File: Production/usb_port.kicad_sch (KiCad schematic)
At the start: 96 parts, among them J401 TYPE-C 16PCB1.6 IP68, Q401 SiZ240DT, Q402 SiZ240DT, U401 TPS25751DREFR, U402 M24512-DFMC6TG, U403 BQ25756RRVR, U404 TPS62933DRLR, U405 TPD6S300RUKR

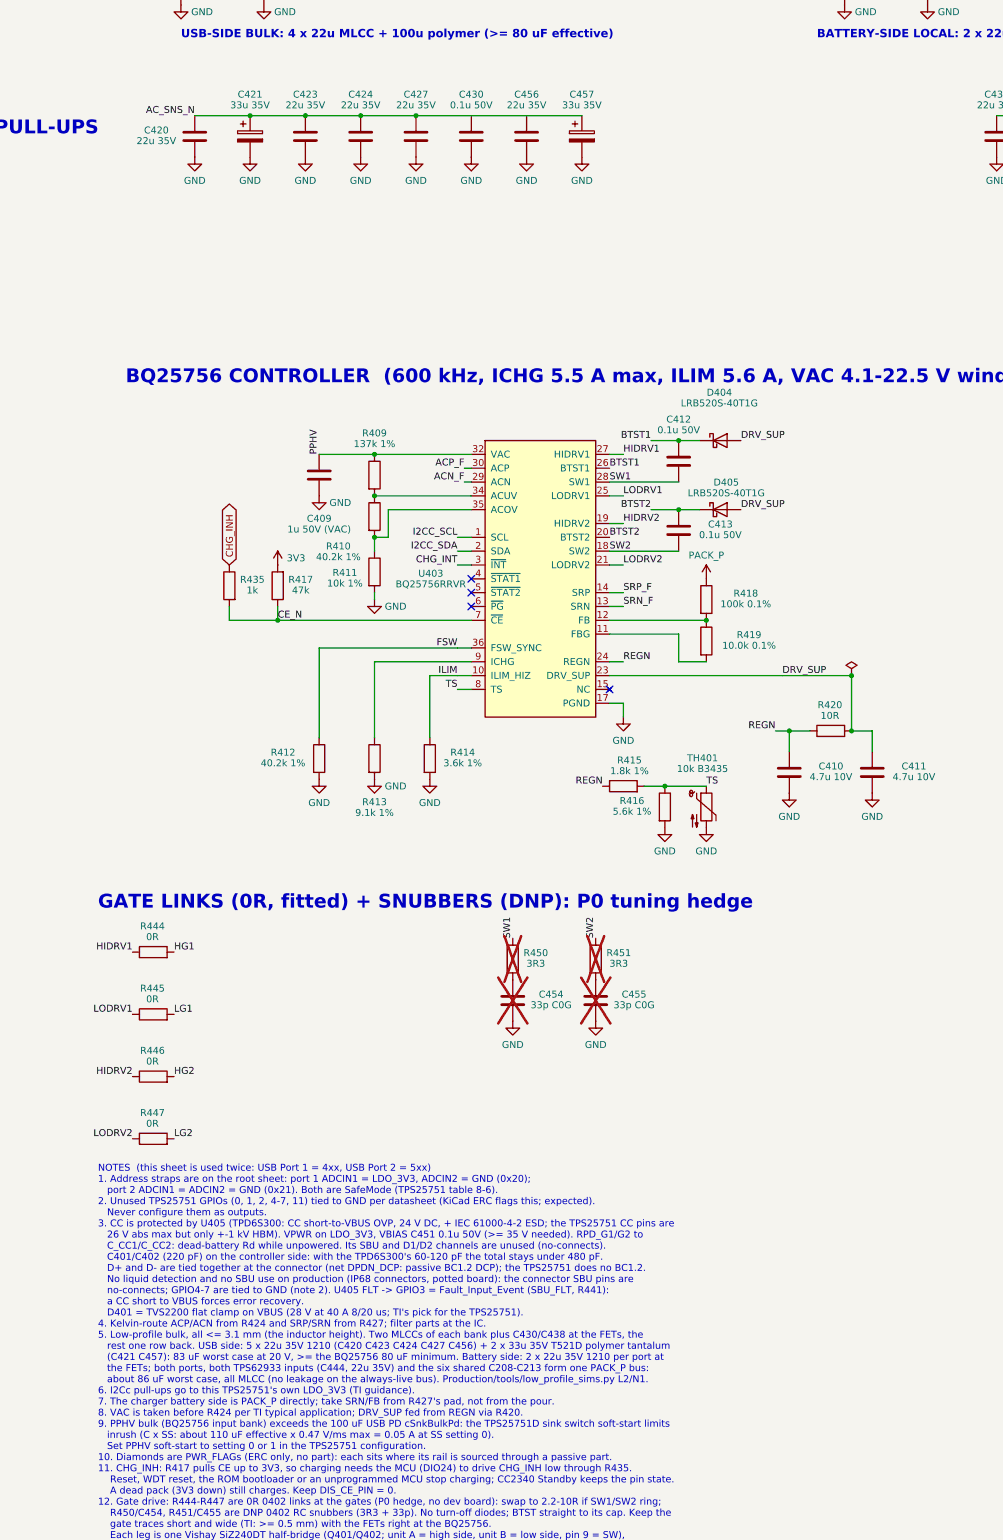
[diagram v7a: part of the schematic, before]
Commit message: Production: C456/C556 -> third T521D 33u (USB bulk 104 uF worst case)
No 33 uF MLCC is stocked in 1210, so the fifth 22u 1210 on each USB side
becomes a third T521D336M035ATE065: 4x 22u 1210 + 3x 33u, 103.7 uF worst at
20 V, worst part 38 %, damping 18.8 dB (low_profile_sims.py L3).

Co-Authored-By: Claude Opus 5.5 <noreply@anthropic.com>
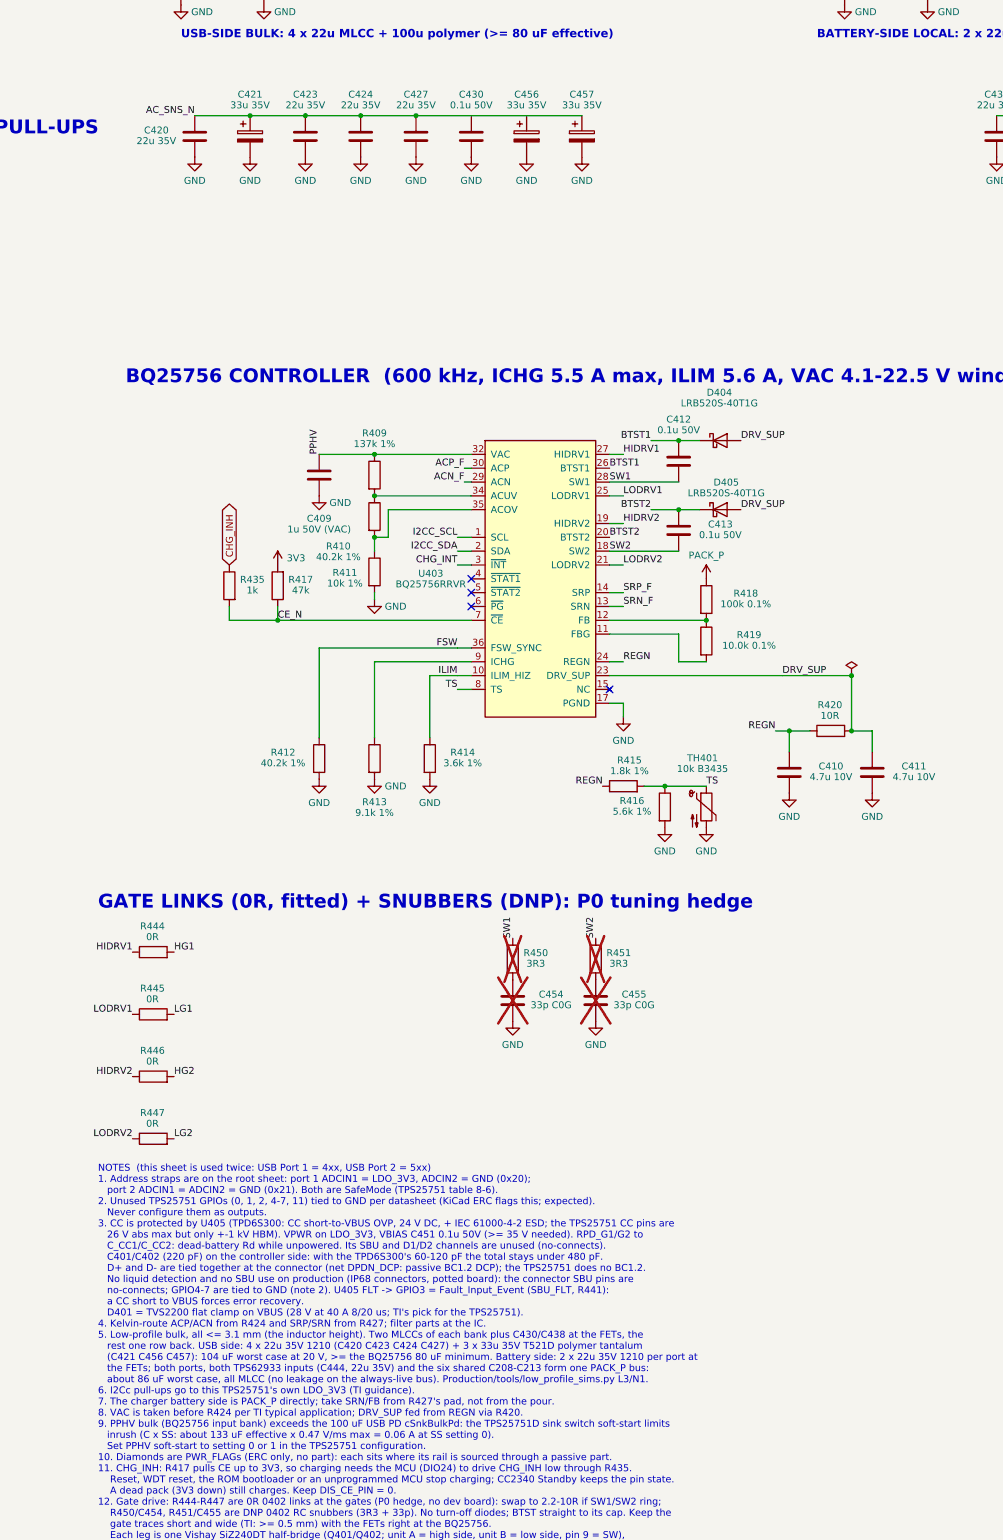
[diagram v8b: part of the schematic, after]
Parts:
- removed C456: 22u 35V, Capacitor_SMD:C_1210_3225Metric, symbol Device:C
- added C456: 33u 35V, Capacitor_Tantalum_SMD:CP_EIA-7343-31_Kemet-D, symbol Device:C_Polarized
- C421: Notes USB-side bulk with C457 (two 33 uF polymer tantalum, 65 mOh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 -> USB-side bulk with C456/C457 (three 33 uF polymer tantalum,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
- C457: Notes Second T521D on AC_SNS_N, see C421 -> T521D on AC_SNS_N with C421, see C421
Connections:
- net AC_SNS_N: now also C456.1
- net GND: now also C456.2
